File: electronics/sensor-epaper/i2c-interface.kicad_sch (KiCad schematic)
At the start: 18 parts, among them Q2 NX2301P, U3 AP3012

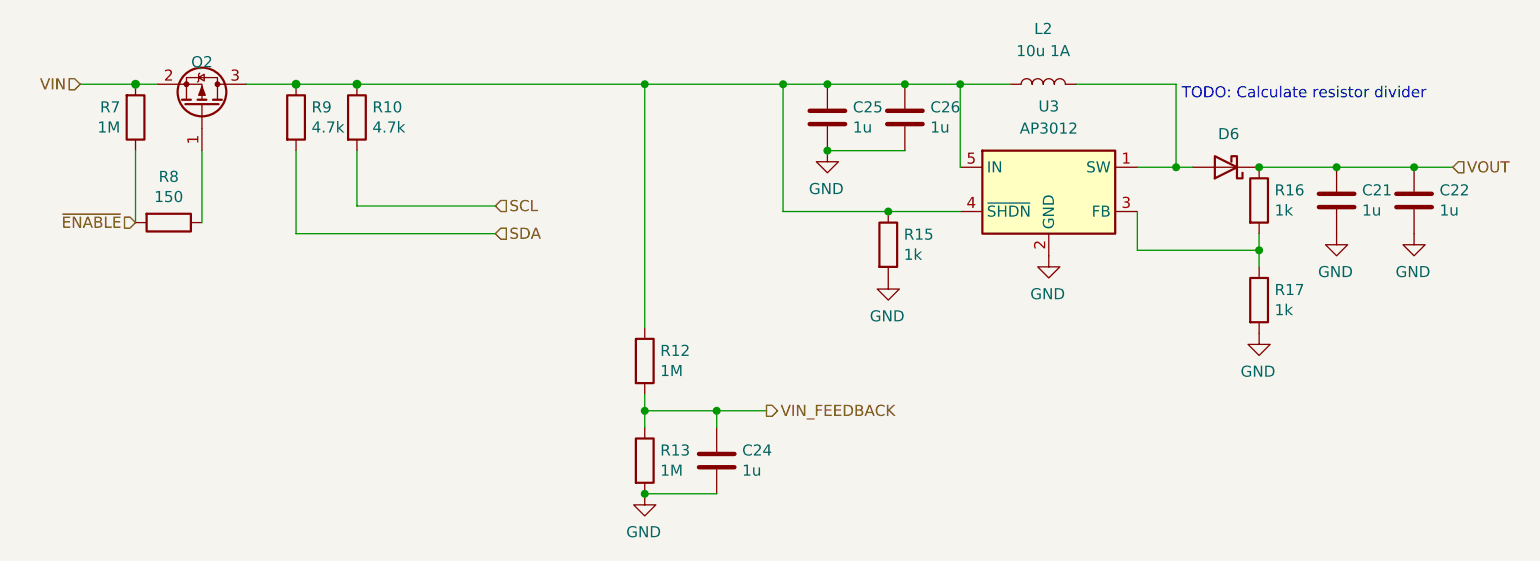
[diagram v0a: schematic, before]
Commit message: Implement fixes for v1.0.0 board: * Fixed mirrored display connector * Fixed wrong button pinout * Remove CS from GPIO11 which is VDD_SPI after all, add a requisite cap * Add tantallum bulk cap, add more capacitance near MCU to counter power gulp related resets using thin USB cable * Consolidate some passive values
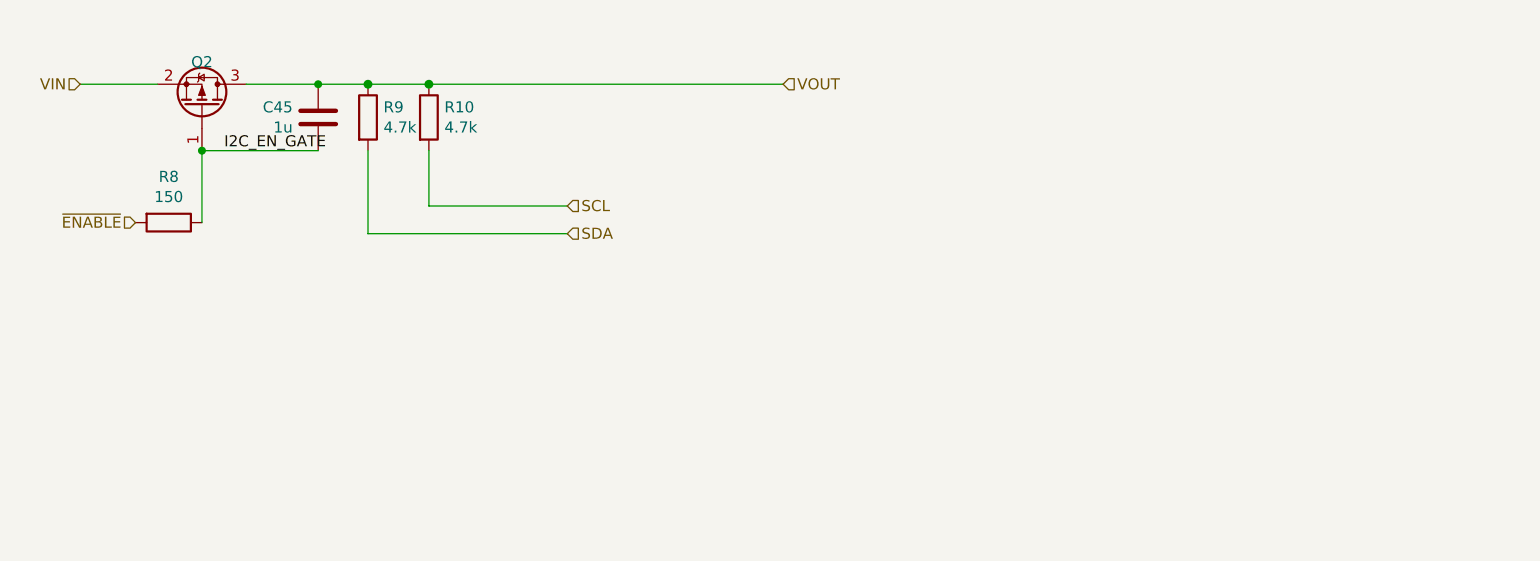
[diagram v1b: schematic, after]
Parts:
- removed C21, C22, C24, C25, C26: 1u, Capacitor_SMD:C_0402_1005Metric, symbol Device:C
- removed D6: MBR0530, Diode_SMD:D_SOD-123, symbol Device:D_Schottky
- removed L2: 10u 1A, Inductor_SMD:L_Taiyo-Yuden_NR-40xx, symbol Device:L
- removed R12, R13, R7: 1M, Resistor_SMD:R_0603_1608Metric, symbol Device:R
- removed R15, R16, R17: 1k, Resistor_SMD:R_0603_1608Metric, symbol Device:R
- removed U3: AP3012, Package_TO_SOT_SMD:SOT-23-5, symbol Regulator_Switching:AP3012
- added C45: 1u, Capacitor_SMD:C_0402_1005Metric, symbol Device:C
- Q2: LCSC C10487 -> C15127
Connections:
- net VOUT: now also Q2.3 (D), R10.1, R9.1, C45.1
- net I2C_EN_GATE: now reaches Q2.1 (G), R8.1
- net I2C_EN_GATE: now also C45.2
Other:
- note removed: "TODO: Calculate resistor divider"
- moved on the sheet: R10, R9
